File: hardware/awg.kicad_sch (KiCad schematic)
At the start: 29 parts, among them U1 LMH6643

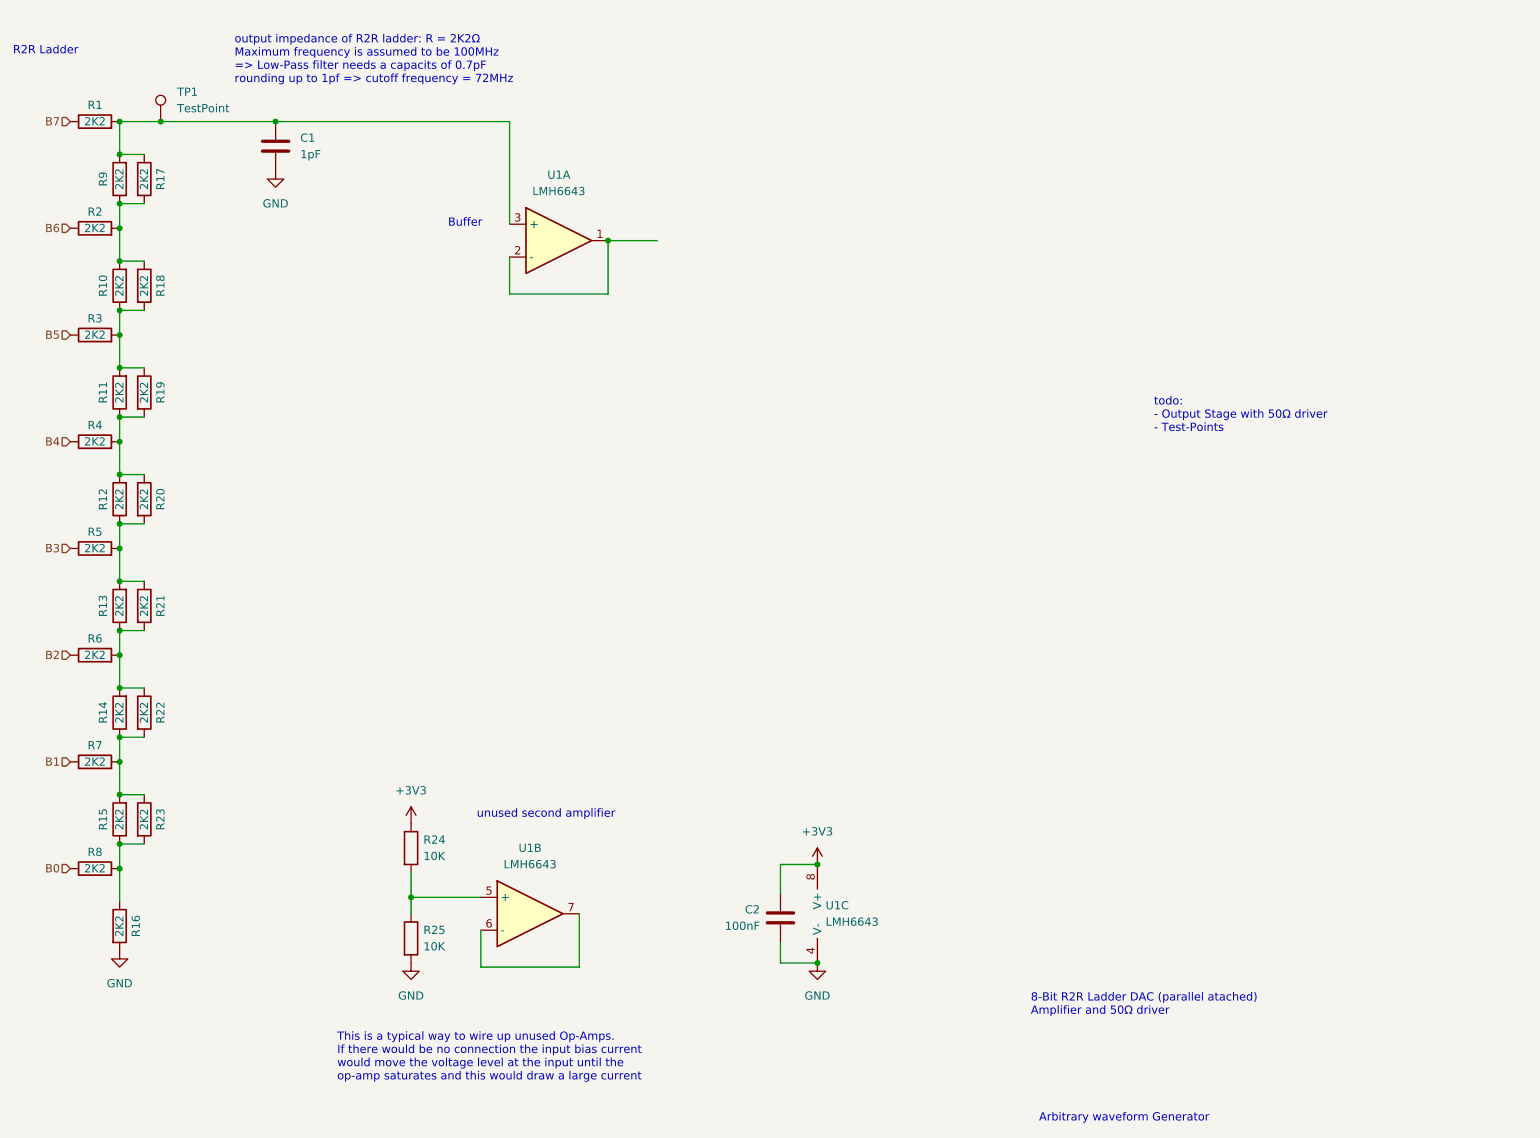
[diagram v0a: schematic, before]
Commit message: [hard] simple dac design ready, integration still missing
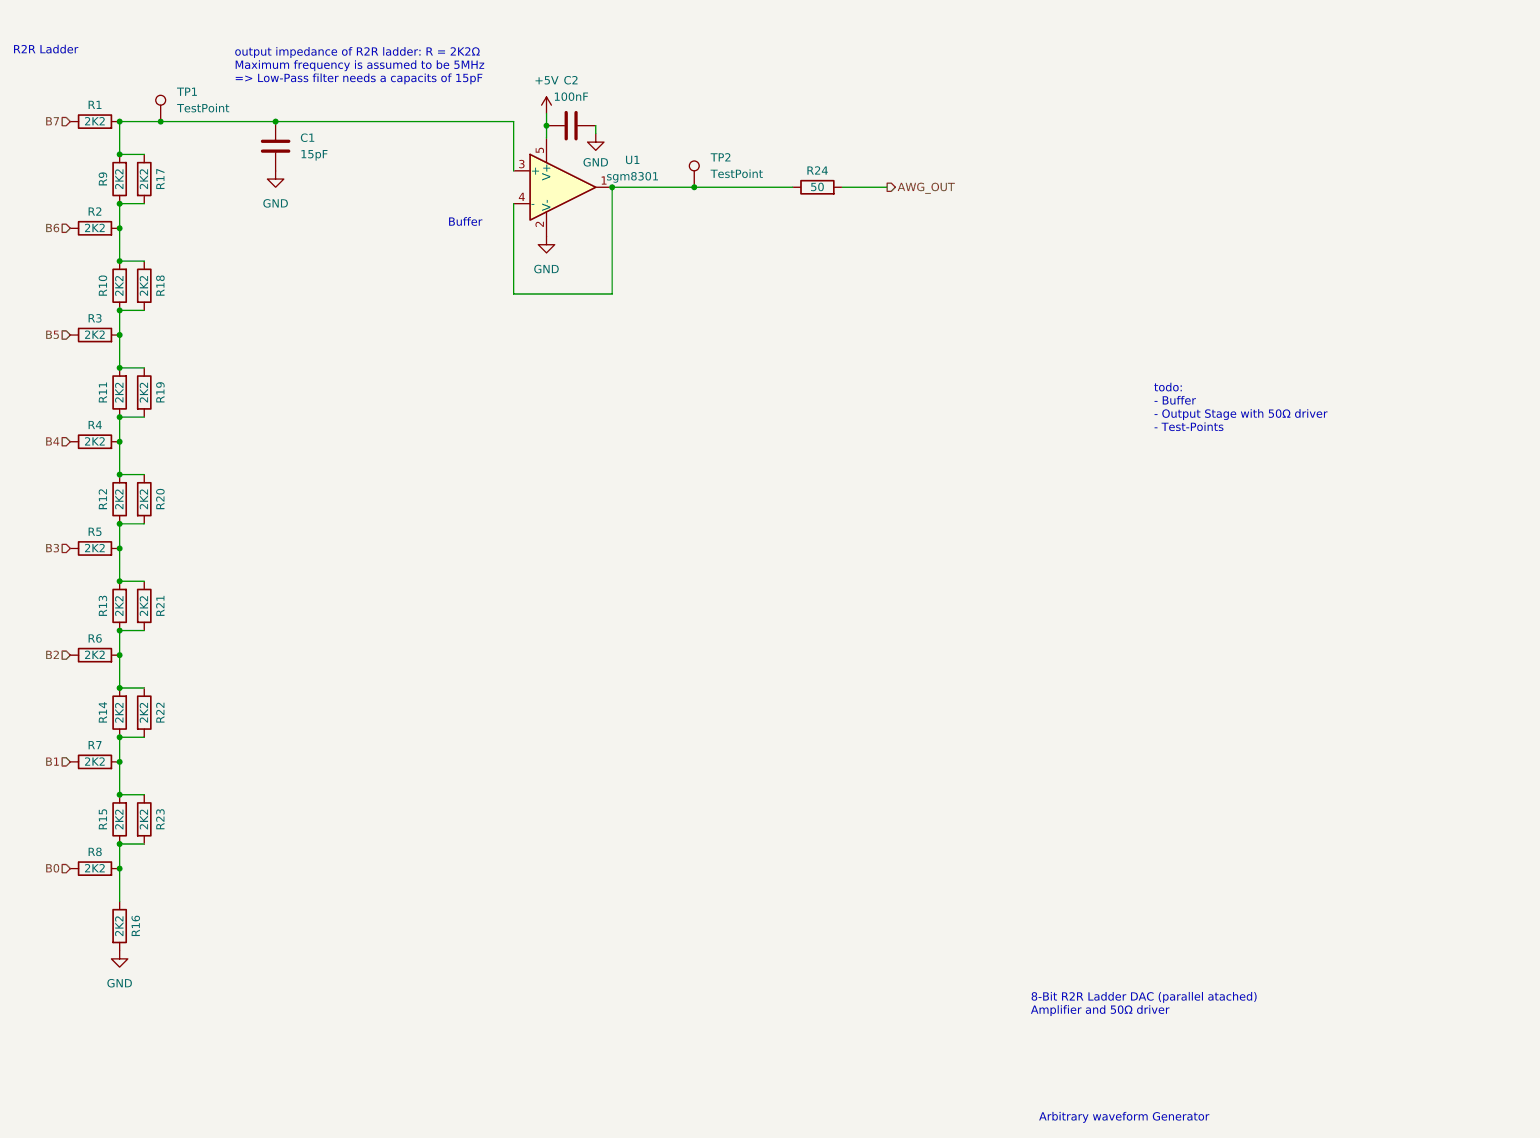
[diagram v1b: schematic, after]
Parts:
- removed R25: 10K, symbol Device:R
- removed U1: LMH6643, symbol symbols:LMH6643
- added TP2: TestPoint, TestPoint:TestPoint_Pad_D1.5mm, symbol Connector:TestPoint
- added U1: sgm8301, Package_TO_SOT_SMD:SOT-23-5, symbol sgm8301:sgm8301
- C1: value 1pF -> 15pF; footprint (none) -> Capacitor_SMD:C_0805_2012Metric_Pad1.18x1.45mm_HandSolder; Reichelt Part-Number RND 1500603N1R0 -> NPO-G0805 15P
- C2: footprint (none) -> Capacitor_SMD:C_0805_2012Metric_Pad1.18x1.45mm_HandSolder; Reichelt Part-Number (none) -> KEM X7R0805 100N
- R1, R10, R11, R12, R13, R14, R15, R16, R17, R18, R19, R2, R20, R21, R22, R23, R3, R4, R5, R6, R7, R8, R9: footprint (none) -> Resistor_SMD:R_0805_2012Metric_Pad1.20x1.40mm_HandSolder
- R24: value 10K -> 50; footprint (none) -> Resistor_SMD:R_0805_2012Metric_Pad1.20x1.40mm_HandSolder; Reichelt Part-Number WAL WR08X1002FTL -> WAL WR08X47R0FTL
- TP1: footprint (none) -> TestPoint:TestPoint_Pad_D1.5mm
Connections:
- net GND: now also U1.2 (V-)
- net at C1.2, R1.2, R17.1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: now also U1.3 (+)
- net AWG_OUT: now reaches R24.2
- net +3V3: no longer names the net of R24.1
- net +3V3: now also TP2.1, U1.1, U1.4 (-); no longer C2.1
- new net +5V: C2.1, U1.5 (V+)
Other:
- note added: "output impedance of R2R ladder: R = 2K2Ω Maximum frequency is assumed to be 5MHz => Low-Pass filter needs a capacits of 15pF"
- note added: "todo: - Buffer - Output Stage with 50Ω driver - Test-Points"
- note removed: "This is a typical way to wire up unused Op-Amps. If there would be no connection the input bias current would move the voltage level at the input until the op-amp saturates and this would draw a large current"
- note removed: "output impedance of R2R ladder: R = 2K2Ω Maximum frequency is assumed to be 100MHz => Low-Pass filter needs a capacits of 0.7pF rounding up to 1pf => cutoff frequency = 72MHz"
- note removed: "todo: - Output Stage with 50Ω driver - Test-Points"
- note removed: "unused second amplifier"

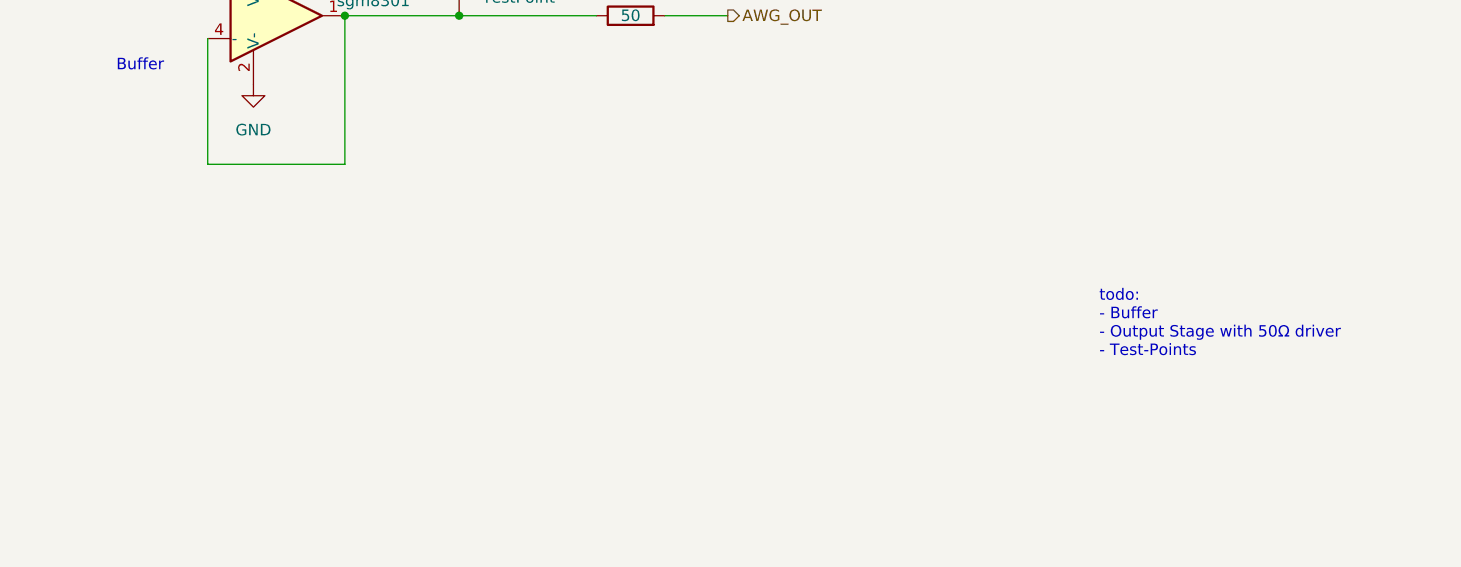
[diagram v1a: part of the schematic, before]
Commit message: [awg] docs and schematics finished but integration not available
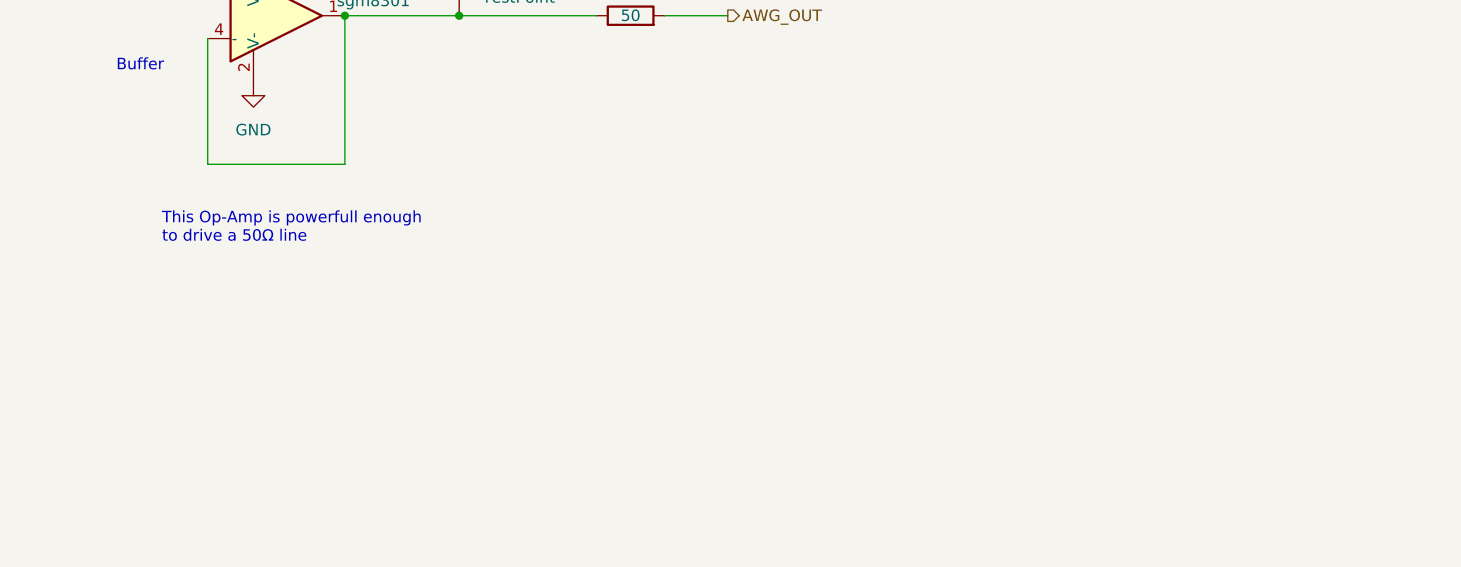
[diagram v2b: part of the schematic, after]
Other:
- note added: "This Op-Amp is powerfull enough to drive a 50Ω line"
- note removed: "todo: - Buffer - Output Stage with 50Ω driver - Test-Points"
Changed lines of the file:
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@@
-    (effects (font (size 1.27 1.27)) (justify left bottom))
-  )
-  (text "todo:\n- Buffer\n- Output Stage with 50Ω driver\n- Test-Points"
-    (at 205.74 83.82 0)
     (effects (font (size 1.27 1.27)) (justify left bottom))
   )
@@
     (effects (font (size 1.27 1.27)) (justify left bottom))
   )
+  (text "This Op-Amp is powerfull enough\nto drive a 50Ω line"
+    (at 101.6 71.12 0)
+    (effects (font (size 1.27 1.27)) (justify left bottom))
+  )

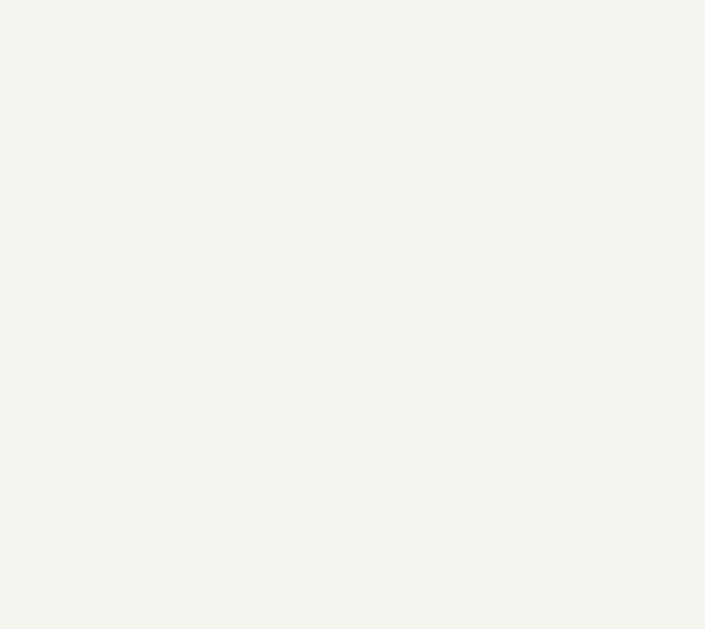
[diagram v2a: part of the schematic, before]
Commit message: update analog front-end and resistor calculator: Better documentation
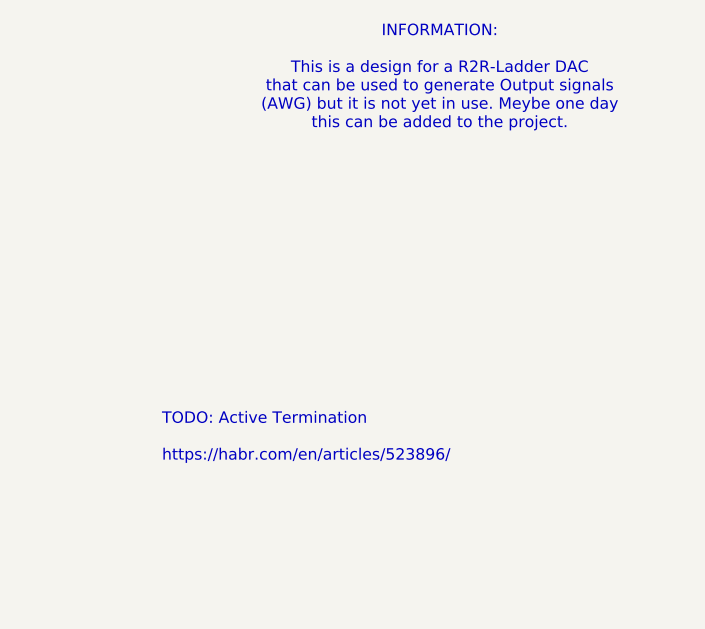
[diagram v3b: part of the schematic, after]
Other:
- note added: "INFORMATION: This is a design for a R2R-Ladder DAC that can be used to generate Output signals (AWG) but it is not yet in use. Meybe one day this can be added to the project."
- note added: "TODO: Active Termination https://habr.com/en/articles/523896/"

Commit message: started PCB routing, AFE ready, rest still in Progress
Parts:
- removed R10, R11, R12, R13, R14, R15, R17, R18, R19, R20, R21, R22, R23: 2K2, Resistor_SMD:R_0805_2012Metric_Pad1.20x1.40mm_HandSolder, symbol Device:R
- added R45, R46, R47, R48, R49, R50: 1k1, Resistor_SMD:R_0805_2012Metric_Pad1.20x1.40mm_HandSolder, symbol Device:R
- R44: renamed from R9; value 2K2 -> 1k1
- renumbered C1 to C18, C2 to C19, R1 to R35, R2 to R36, R3 to R37, R4 to R38, R5 to R39, R6 to R40, R7 to R41, R8 to R42, R16 to R43, R24 to R51, TP1 to TP19, TP2 to TP20, U1 to U6
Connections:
- net at R39.2: now also R47.1, R48.2
- net at R42.2, R43.1: now also R50.1
- net at R41.2: now also R49.1, R50.2
- net at R40.2: now also R48.1, R49.2
- net at R37.2: now also R45.1, R46.2
- net at R38.2: now also R46.1, R47.2
- net at R36.2, R44.1: now also R45.2
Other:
- note added: "INFORMATION: This design was never intended to be used in this project. However, it came out to be working good enough under a High Z load that it can be considered usefull."
- note added: "This Op-Amp is hopefully powerfull enough to drive a 50Ω line. Maybe it would be better to switch to 600Ω?"
- note removed: "INFORMATION: This is a design for a R2R-Ladder DAC that can be used to generate Output signals (AWG) but it is not yet in use. Meybe one day this can be added to the project."
- note removed: "R2R Ladder"
- note removed: "TODO: Active Termination https://habr.com/en/articles/523896/"
- note removed: "This Op-Amp is powerfull enough to drive a 50Ω line"
- moved on the sheet: R43

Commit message: Hardware: now in the state where a testing prototype can be ordered
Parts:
- renumbered TP19 to TP6, TP20 to TP7
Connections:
- net +5V renamed +3V3
